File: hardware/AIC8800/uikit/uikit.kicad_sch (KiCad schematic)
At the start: 36 parts, among them J1 Conn_01x20, J2 Conn_01x20, J3 Conn_01x10, J4 Conn_01x06, J5 USB_C_Receptacle_USB2.0, J6 Micro_SD_Card, J7 PJ-393-USA, U1 AIC1000A, U2 CH340N

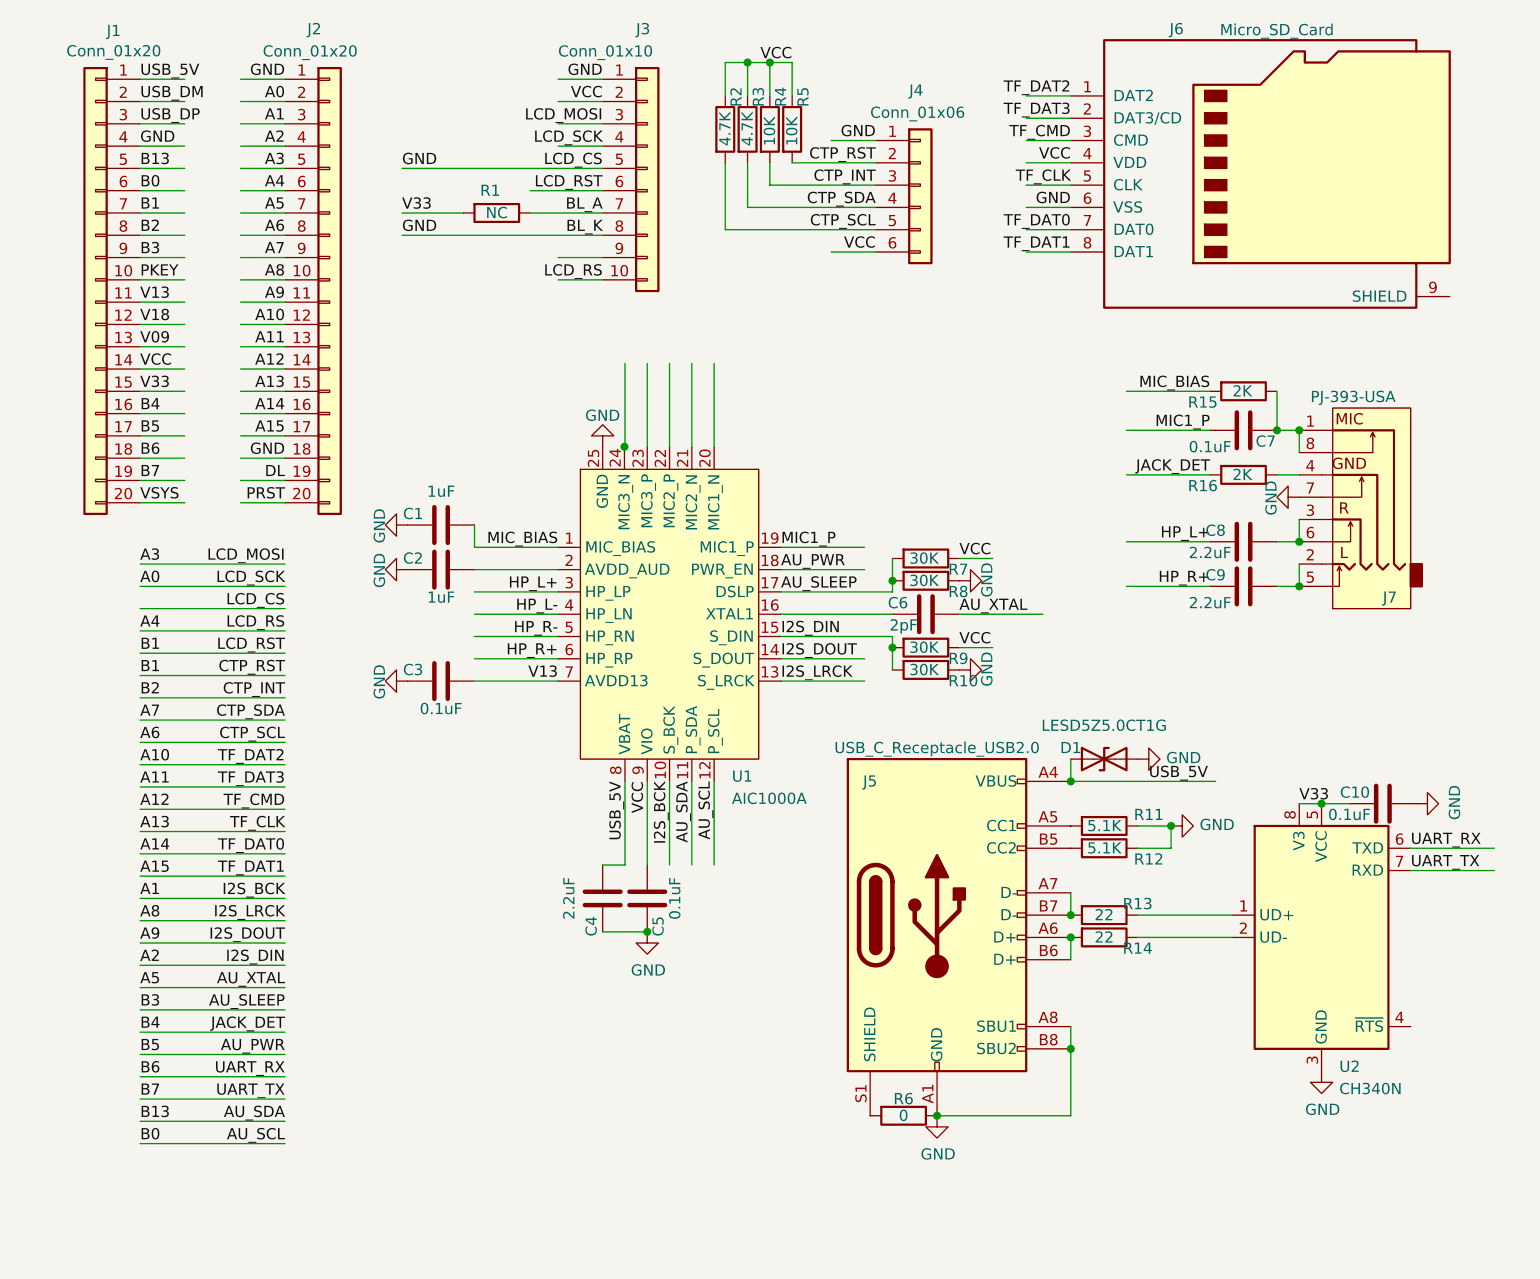
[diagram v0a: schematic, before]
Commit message: [hardware/AIC8800/uikit] update PCB
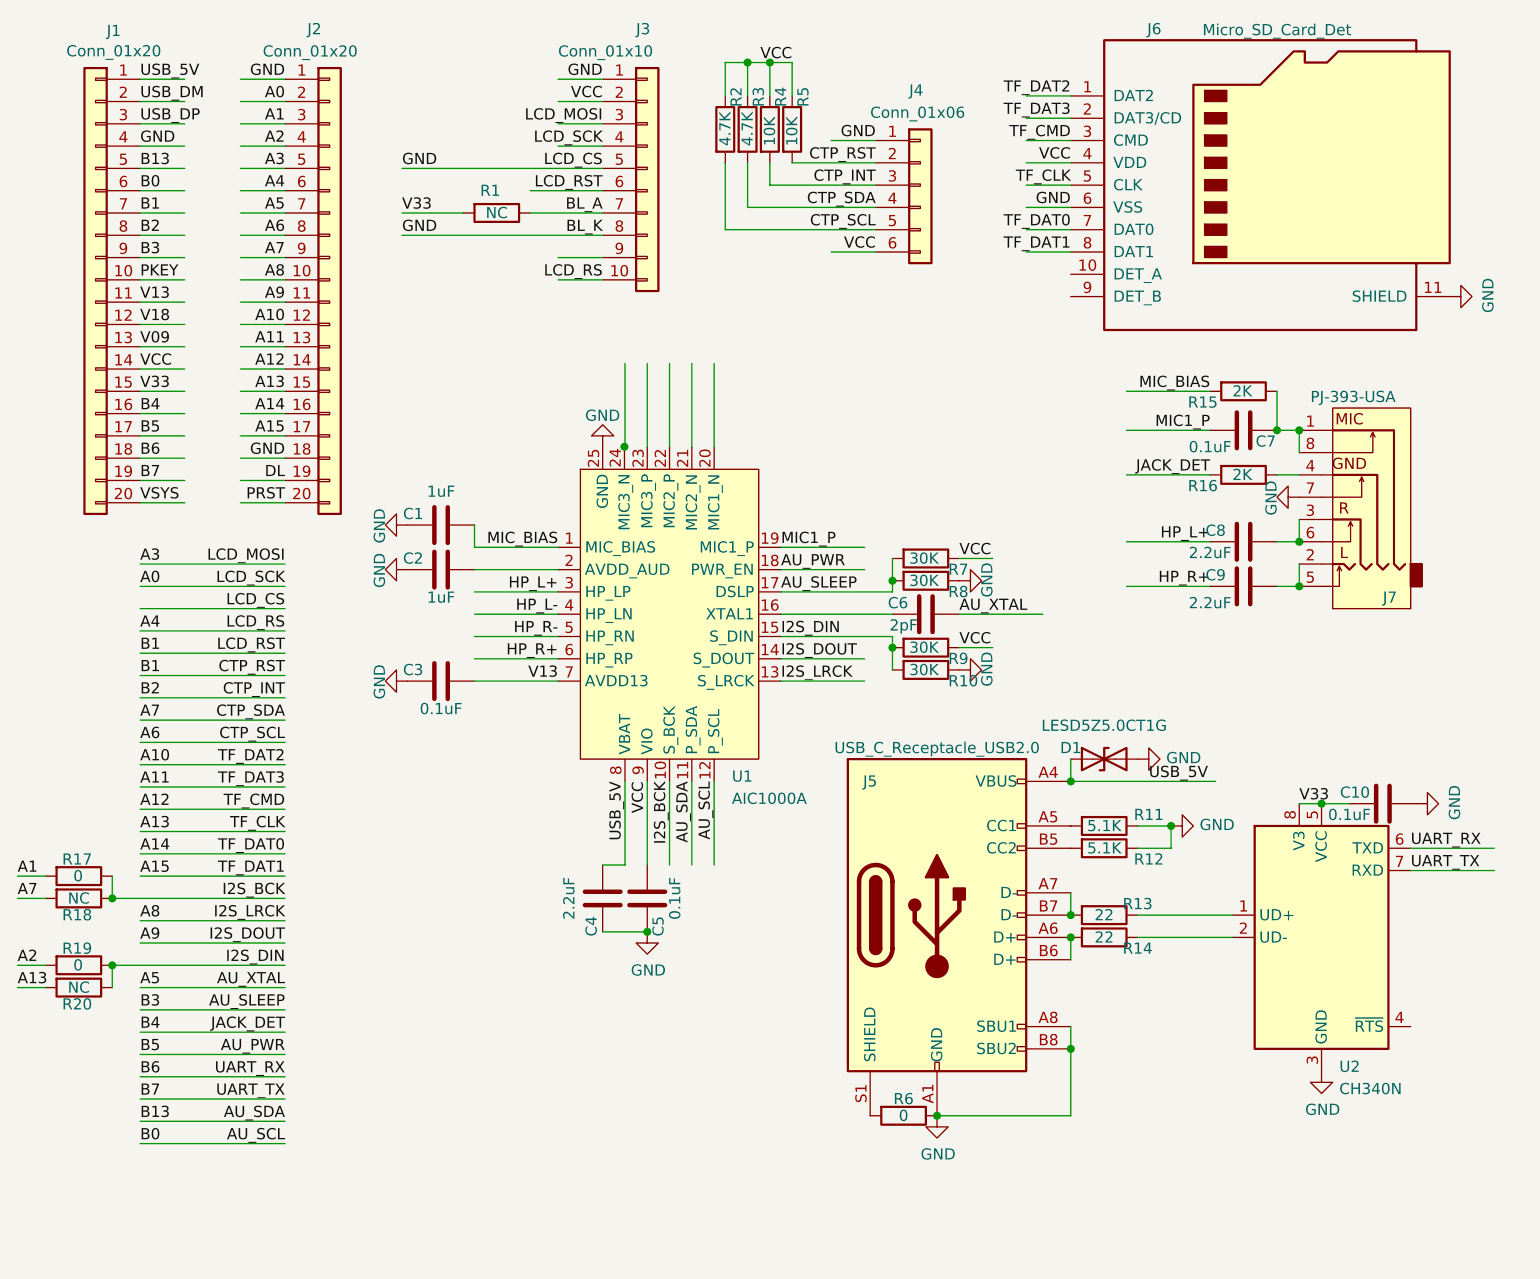
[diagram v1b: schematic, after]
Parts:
- removed J6: Micro_SD_Card, Connector_Card:microSD_HC_Wuerth_693072010801, symbol Connector:Micro_SD_Card
- added J6: Micro_SD_Card_Det, Connector_Card:microSD_HC_Molex_104031-0811, symbol Connector:Micro_SD_Card_Det
- added R17, R19: 0, Resistor_SMD:R_0402_1005Metric, symbol Device:R
- added R18, R20: NC, Resistor_SMD:R_0402_1005Metric, symbol Device:R
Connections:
- net A1: now also R17.2; no longer U1.10 (S_BCK)
- net A10: now also J6.1 (DAT2)
- net A11: now also J6.2 (DAT3/CD)
- net A12: now also J6.3 (CMD)
- net A13: now also J6.5 (CLK), R20.2
- net A14: now also J6.7 (DAT0)
- net A15: now also J6.8 (DAT1)
- net A2: now also R19.2; no longer R10.2, R9.2, U1.15 (S_DIN)
- net A7: now also R18.2
- net GND: now also J6.11 (SHIELD), J6.6 (VSS)
- net VCC: now also J6.4 (VDD)
- new net I2S_BCK: R17.1, R18.1, U1.10 (S_BCK)
- new net I2S_DIN: R10.2, R19.1, R20.1, R9.2, U1.15 (S_DIN)

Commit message: [hardware/AIC8800/uikit] update PCB
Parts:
- J3: footprint Connector_FFC-FPC:Hirose_FH12-10S-0.5SH_1x10-1MP_P0.50mm_Horizontal -> VSF:Hirose_FH12-10S-0.5SH_1x10-1MP_P0.50mm_Horizontal_Reverse
- J4: footprint Connector_FFC-FPC:Hirose_FH12-6S-0.5SH_1x06-1MP_P0.50mm_Horizontal -> VSF:Hirose_FH12-6S-0.5SH_1x06-1MP_P0.50mm_Horizontal_Reverse
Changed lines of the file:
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@@
       (effects (font (size 1.27 1.27)) (justify left))
     )
-    (property "Footprint" "Connector_FFC-FPC:Hirose_FH12-6S-0.5SH_1x06-1MP_P0.50mm_Horizontal" (id 2) (at 120.65 38.735 0)
+    (property "Footprint" "VSF:Hirose_FH12-6S-0.5SH_1x06-1MP_P0.50mm_Horizontal_Reverse" (id 2) (at 120.65 38.735 0)
       (effects (font (size 1.27 1.27)) hide)
     )
@@
       (effects (font (size 1.27 1.27)) (justify left))
     )
-    (property "Footprint" "Connector_FFC-FPC:Hirose_FH12-10S-0.5SH_1x10-1MP_P0.50mm_Horizontal" (id 2) (at 89.535 36.83 0)
+    (property "Footprint" "VSF:Hirose_FH12-10S-0.5SH_1x10-1MP_P0.50mm_Horizontal_Reverse" (id 2) (at 89.535 36.83 0)
       (effects (font (size 1.27 1.27)) hide)
     )
@@
   (symbol (lib_id "power:GND") (at 180.975 51.435 90) (unit 1)
     (in_bom yes) (on_board yes)
-    (property "Reference" "#PWR?" (id 0) (at 187.325 51.435 0)
+    (property "Reference" "#PWR0102" (id 0) (at 187.325 51.435 0)
       (effects (font (size 1.27 1.27)) hide)
     )
@@
     )
     (path "/f0527ce6-54eb-44ec-8b40-f12bfb912173"
-      (reference "#PWR?") (unit 1) (value "GND") (footprint "")
+      (reference "#PWR0102") (unit 1) (value "GND") (footprint "")
     )
     (path "/faf7f873-d004-44e5-b2bd-9d7562f28cb5"
@@
     )
     (path "/e204a6c5-45d9-4fa4-b41f-d94e47c3560c"
-      (reference "J3") (unit 1) (value "Conn_01x10") (footprint "Connector_FFC-FPC:Hirose_FH12-10S-0.5SH_1x10-1MP_P0.50mm_Horizontal")
+      (reference "J3") (unit 1) (value "Conn_01x10") (footprint "VSF:Hirose_FH12-10S-0.5SH_1x10-1MP_P0.50mm_Horizontal_Reverse")
     )
     (path "/7e3b4dd4-b83a-4efe-a2fa-f2570d41b3e3"
-      (reference "J4") (unit 1) (value "Conn_01x06") (footprint "Connector_FFC-FPC:Hirose_FH12-6S-0.5SH_1x06-1MP_P0.50mm_Horizontal")
+      (reference "J4") (unit 1) (value "Conn_01x06") (footprint "VSF:Hirose_FH12-6S-0.5SH_1x06-1MP_P0.50mm_Horizontal_Reverse")
     )
     (path "/f7e476c6-81a9-4c32-8e43-9df3cee2cd9a"

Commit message: [hardware/aic8800/uikit] update
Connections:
- net USB_5V: now also U2.5 (VCC)
- net V33: no longer C10.1, R1.2, U2.5 (VCC), U2.8 (V3)
- net at U2.1 (UD+): now also R14.1; no longer R13.1
- net at U2.2 (UD-): now also R13.1; no longer R14.1
- new net USB_3V: C10.1, R1.2, U2.8 (V3)
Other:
- moved on the sheet: C10
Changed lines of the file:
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@@
 (kicad_sch (version 20211123) (generator eeschema)
   (paper "A4")
-  (junction (at 166.37 109.22) (diameter 0) (color 0 0 0 0)
-  )
   (junction (at 103.505 24.765) (diameter 0) (color 0 0 0 0)
   )
@@
     (stroke (width 0) (type default) (color 0 0 0 0))
   )
+  (wire (pts (xy 156.21 121.92) (xy 151.765 121.92))
+    (stroke (width 0) (type default) (color 0 0 0 0))
+  )
   (wire (pts (xy 100.965 41.275) (xy 115.57 41.275))
     (stroke (width 0) (type default) (color 0 0 0 0))
@@
     (stroke (width 0) (type default) (color 0 0 0 0))
   )
-  (wire (pts (xy 166.37 109.22) (xy 169.545 109.22))
-    (stroke (width 0) (type default) (color 0 0 0 0))
-  )
   (wire (pts (xy 137.795 144.78) (xy 137.795 137.16))
     (stroke (width 0) (type default) (color 0 0 0 0))
@@
     (stroke (width 0) (type default) (color 0 0 0 0))
   )
-  (wire (pts (xy 145.415 121.92) (xy 156.21 121.92))
-    (stroke (width 0) (type default) (color 0 0 0 0))
-  )
   (wire (pts (xy 104.775 87.63) (xy 117.475 87.63))
     (stroke (width 0) (type default) (color 0 0 0 0))
@@
     (stroke (width 0) (type default) (color 0 0 0 0))
   )
+  (wire (pts (xy 149.225 123.19) (xy 151.765 123.19))
+    (stroke (width 0) (type default) (color 0 0 0 0))
+  )
   (wire (pts (xy 31.75 104.775) (xy 48.26 104.775))
     (stroke (width 0) (type default) (color 0 0 0 0))
   )
-  (wire (pts (xy 145.415 124.46) (xy 156.21 124.46))
+  (wire (pts (xy 166.37 109.22) (xy 173.355 109.22))
     (stroke (width 0) (type default) (color 0 0 0 0))
   )
@@
     (stroke (width 0) (type default) (color 0 0 0 0))
   )
-  (wire (pts (xy 163.83 109.22) (xy 166.37 109.22))
-    (stroke (width 0) (type default) (color 0 0 0 0))
-  )
   (wire (pts (xy 163.83 81.915) (xy 163.83 84.455))
     (stroke (width 0) (type default) (color 0 0 0 0))
@@
     (stroke (width 0) (type default) (color 0 0 0 0))
   )
+  (wire (pts (xy 163.83 104.14) (xy 163.83 109.22))
+    (stroke (width 0) (type default) (color 0 0 0 0))
+  )
   (wire (pts (xy 104.775 95.25) (xy 114.3 95.25))
     (stroke (width 0) (type default) (color 0 0 0 0))
@@
     (stroke (width 0) (type default) (color 0 0 0 0))
   )
+  (wire (pts (xy 163.83 104.14) (xy 175.895 104.14))
+    (stroke (width 0) (type default) (color 0 0 0 0))
+  )
   (wire (pts (xy 161.29 71.755) (xy 163.83 71.755))
     (stroke (width 0) (type default) (color 0 0 0 0))
@@
     (stroke (width 0) (type default) (color 0 0 0 0))
   )
+  (wire (pts (xy 149.225 124.46) (xy 149.225 123.19))
+    (stroke (width 0) (type default) (color 0 0 0 0))
+  )
   (wire (pts (xy 137.795 33.655) (xy 132.715 33.655))
     (stroke (width 0) (type default) (color 0 0 0 0))
@@
     (stroke (width 0) (type default) (color 0 0 0 0))
   )
+  (wire (pts (xy 151.765 121.92) (xy 151.765 123.19))
+    (stroke (width 0) (type default) (color 0 0 0 0))
+  )
   (wire (pts (xy 103.505 24.765) (xy 106.045 24.765))
     (stroke (width 0) (type default) (color 0 0 0 0))
@@
     (stroke (width 0) (type default) (color 0 0 0 0))
   )
+  (wire (pts (xy 150.495 121.92) (xy 150.495 124.46))
+    (stroke (width 0) (type default) (color 0 0 0 0))
+  )
   (wire (pts (xy 48.26 31.75) (xy 43.18 31.75))
     (stroke (width 0) (type default) (color 0 0 0 0))
@@
     (stroke (width 0) (type default) (color 0 0 0 0))
   )
+  (wire (pts (xy 150.495 124.46) (xy 156.21 124.46))
+    (stroke (width 0) (type default) (color 0 0 0 0))
+  )
   (wire (pts (xy 17.78 127.635) (xy 20.955 127.635))
     (stroke (width 0) (type default) (color 0 0 0 0))
@@
     (stroke (width 0) (type default) (color 0 0 0 0))
   )
+  (wire (pts (xy 145.415 124.46) (xy 149.225 124.46))
+    (stroke (width 0) (type default) (color 0 0 0 0))
+  )
   (wire (pts (xy 61.595 41.91) (xy 68.58 41.91))
     (stroke (width 0) (type default) (color 0 0 0 0))
@@
     (stroke (width 0) (type default) (color 0 0 0 0))
   )
+  (wire (pts (xy 145.415 121.92) (xy 150.495 121.92))
+    (stroke (width 0) (type default) (color 0 0 0 0))
+  )
   (wire (pts (xy 31.75 109.855) (xy 48.26 109.855))
     (stroke (width 0) (type default) (color 0 0 0 0))
@@
     (effects (font (size 1.27 1.27)) (justify right bottom))
   )
-  (label "V33" (at 163.83 109.22 0)
+  (label "USB_3V" (at 163.83 104.14 0)
     (effects (font (size 1.27 1.27)) (justify left bottom))
   )
@@
     (effects (font (size 1.27 1.27)) (justify right bottom))
   )
-  (label "V33" (at 61.595 41.91 0)
-    (effects (font (size 1.27 1.27)) (justify left bottom))
-  )
   (label "B3" (at 31.75 132.715 0)
     (effects (font (size 1.27 1.27)) (justify left bottom))
@@
     (effects (font (size 1.27 1.27)) (justify left bottom))
   )
+  (label "USB_3V" (at 61.595 41.91 0)
+    (effects (font (size 1.27 1.27)) (justify left bottom))
+  )
   (label "AU_SCL" (at 97.155 106.68 270)
     (effects (font (size 1.27 1.27)) (justify right bottom))
@@
   (label "TF_DAT2" (at 137.795 28.575 180)
     (effects (font (size 1.27 1.27)) (justify right bottom))
+  )
+  (label "USB_5V" (at 166.37 109.22 0)
+    (effects (font (size 1.27 1.27)) (justify left bottom))
   )
   (symbol (lib_id "Device:C") (at 157.48 84.455 90) (unit 1)
@@
     (pin "2")
   )
-  (symbol (lib_id "power:GND") (at 177.165 109.22 90) (unit 1)
-    (in_bom yes) (on_board yes)
-    (property "Reference" "#PWR012" (id 0) (at 183.515 109.22 0)
-      (effects (font (size 1.27 1.27)) hide)
-    )
-    (property "Value" "GND" (id 1) (at 181.5592 109.093 0))
-    (property "Footprint" "" (id 2) (at 177.165 109.22 0)
-      (effects (font (size 1.27 1.27)) hide)
-    )
-    (property "Datasheet" "" (id 3) (at 177.165 109.22 0)
+  (symbol (lib_id "power:GND") (at 183.515 104.14 90) (unit 1)
+    (in_bom yes) (on_board yes)
+    (property "Reference" "#PWR012" (id 0) (at 189.865 104.14 0)
+      (effects (font (size 1.27 1.27)) hide)
+    )
+    (property "Value" "GND" (id 1) (at 187.9092 104.013 0))
+    (property "Footprint" "" (id 2) (at 183.515 104.14 0)
+      (effects (font (size 1.27 1.27)) hide)
+    )
+    (property "Datasheet" "" (id 3) (at 183.515 104.14 0)
       (effects (font (size 1.27 1.27)) hide)
     )
@@
   (symbol (lib_id "Device:R") (at 141.605 121.92 270) (unit 1)
     (in_bom yes) (on_board yes)
-    (property "Reference" "R13" (id 0) (at 145.415 120.65 90))
+    (property "Reference" "R13" (id 0) (at 146.05 120.65 90))
     (property "Value" "22" (id 1) (at 141.605 121.92 90))
     (property "Footprint" "Resistor_SMD:R_0402_1005Metric" (id 2) (at 141.605 120.142 90)
@@
     (pin "2")
   )
-  (symbol (lib_id "Device:C") (at 173.355 109.22 90) (unit 1)
-    (in_bom yes) (on_board yes)
-    (property "Reference" "C10" (id 0) (at 170.18 107.95 90))
-    (property "Value" "0.1uF" (id 1) (at 169.545 110.49 90))
-    (property "Footprint" "Capacitor_SMD:C_0402_1005Metric" (id 2) (at 177.165 108.2548 0)
-      (effects (font (size 1.27 1.27)) hide)
-    )
-    (property "Datasheet" "~" (id 3) (at 173.355 109.22 0)
+  (symbol (lib_id "Device:C") (at 179.705 104.14 90) (unit 1)
+    (in_bom yes) (on_board yes)
+    (property "Reference" "C10" (id 0) (at 176.53 102.87 90))
+    (property "Value" "0.1uF" (id 1) (at 175.895 105.41 90))
+    (property "Footprint" "Capacitor_SMD:C_0402_1005Metric" (id 2) (at 183.515 103.1748 0)
+      (effects (font (size 1.27 1.27)) hide)
+    )
+    (property "Datasheet" "~" (id 3) (at 179.705 104.14 0)
       (effects (font (size 1.27 1.27)) hide)
     )
@@
   (symbol (lib_id "Device:R") (at 141.605 124.46 270) (unit 1)
     (in_bom yes) (on_board yes)
-    (property "Reference" "R14" (id 0) (at 145.415 125.73 90))
+    (property "Reference" "R14" (id 0) (at 146.05 125.73 90))
     (property "Value" "22" (id 1) (at 141.605 124.46 90))
     (property "Footprint" "Resistor_SMD:R_0402_1005Metric" (id 2) (at 141.605 122.682 90)

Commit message: [hardware/aic8800/uikit] PB6/PB7 can not be used as uart
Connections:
- net AU_SLEEP: now also J1.7 (Pin_7); no longer J1.9 (Pin_9)
- net B2: now also U2.6 (TXD); no longer J4.3 (Pin_3), R4.2
- net B6: now also J4.3 (Pin_3), R4.2; no longer U2.6 (TXD)
- net B7: now also J3.6 (Pin_6), J4.2 (Pin_2), R5.2; no longer U2.7 (RXD)
- removed net B1: J1.7 (Pin_7), J3.6 (Pin_6), J4.2 (Pin_2), R5.2
- new net B3: J1.9 (Pin_9), U2.7 (RXD)
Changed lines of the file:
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@@
     (effects (font (size 1.27 1.27)) (justify right bottom))
-  )
-  (label "B1" (at 31.75 94.615 0)
-    (effects (font (size 1.27 1.27)) (justify left bottom))
   )
   (label "B5" (at 31.75 137.795 0)
@@
     (effects (font (size 1.27 1.27)) (justify right bottom))
   )
-  (label "B2" (at 31.75 97.155 0)
+  (label "B2" (at 31.75 140.335 0)
     (effects (font (size 1.27 1.27)) (justify left bottom))
   )
@@
     (effects (font (size 1.27 1.27)) (justify right bottom))
   )
-  (label "B3" (at 31.75 132.715 0)
+  (label "B3" (at 31.75 142.875 0)
     (effects (font (size 1.27 1.27)) (justify left bottom))
   )
@@
     (effects (font (size 1.27 1.27)) (justify left bottom))
   )
-  (label "B1" (at 31.75 92.075 0)
+  (label "B1" (at 31.75 132.715 0)
     (effects (font (size 1.27 1.27)) (justify left bottom))
   )
@@
     (effects (font (size 1.27 1.27)) (justify right bottom))
   )
-  (label "B6" (at 31.75 140.335 0)
+  (label "B6" (at 31.75 97.155 0)
     (effects (font (size 1.27 1.27)) (justify left bottom))
   )
@@
     (effects (font (size 1.27 1.27)) (justify right bottom))
   )
-  (label "B7" (at 31.75 142.875 0)
+  (label "B7" (at 31.75 92.075 0)
     (effects (font (size 1.27 1.27)) (justify left bottom))
   )
@@
     (effects (font (size 1.27 1.27)) (justify left bottom))
   )
+  (label "B7" (at 31.75 94.615 0)
+    (effects (font (size 1.27 1.27)) (justify left bottom))
+  )
